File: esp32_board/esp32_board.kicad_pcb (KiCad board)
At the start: 2 copper layers, 57.2 x 63.5 mm, 6 parts, among them J1 Conn_01x06, Q1 2N5551, Q2 IRF5305

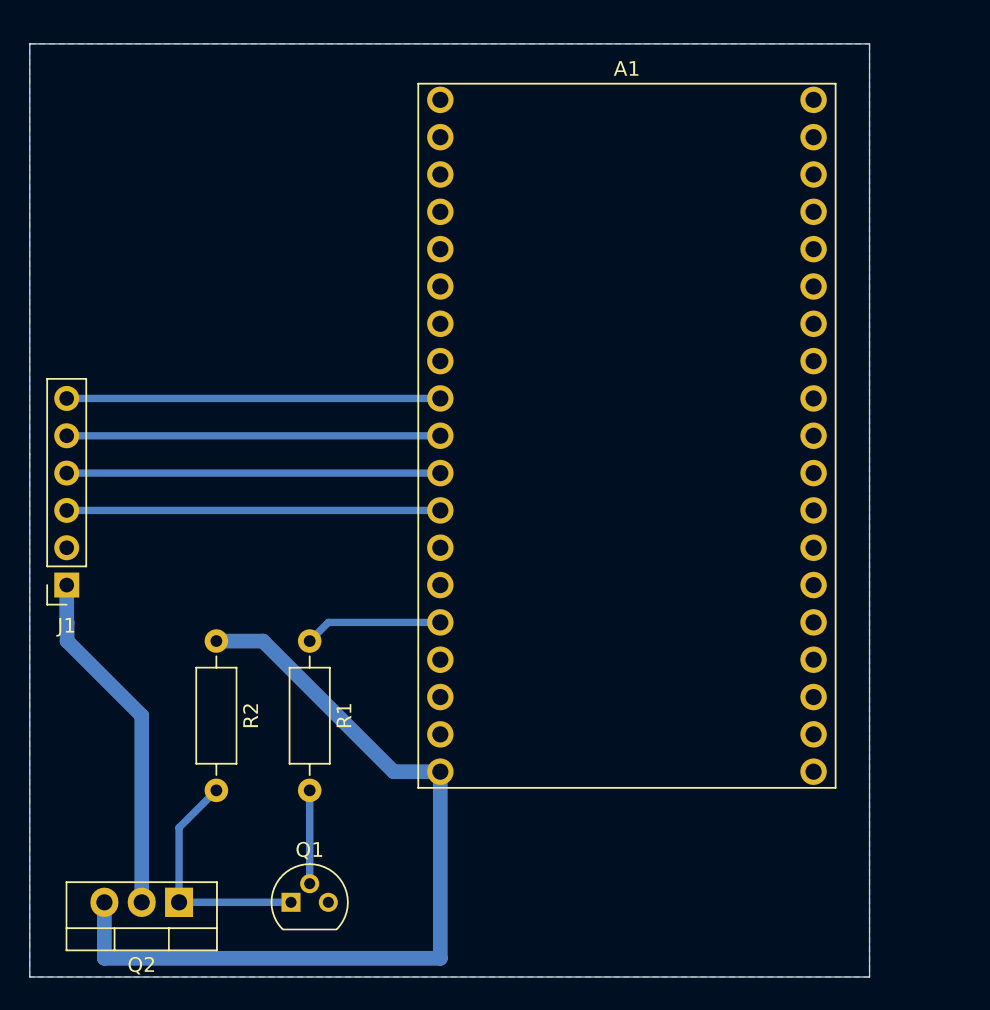
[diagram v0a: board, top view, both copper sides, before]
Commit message: Reduce PCB size to 50mmx50mm, set zone clearance to 1 mm
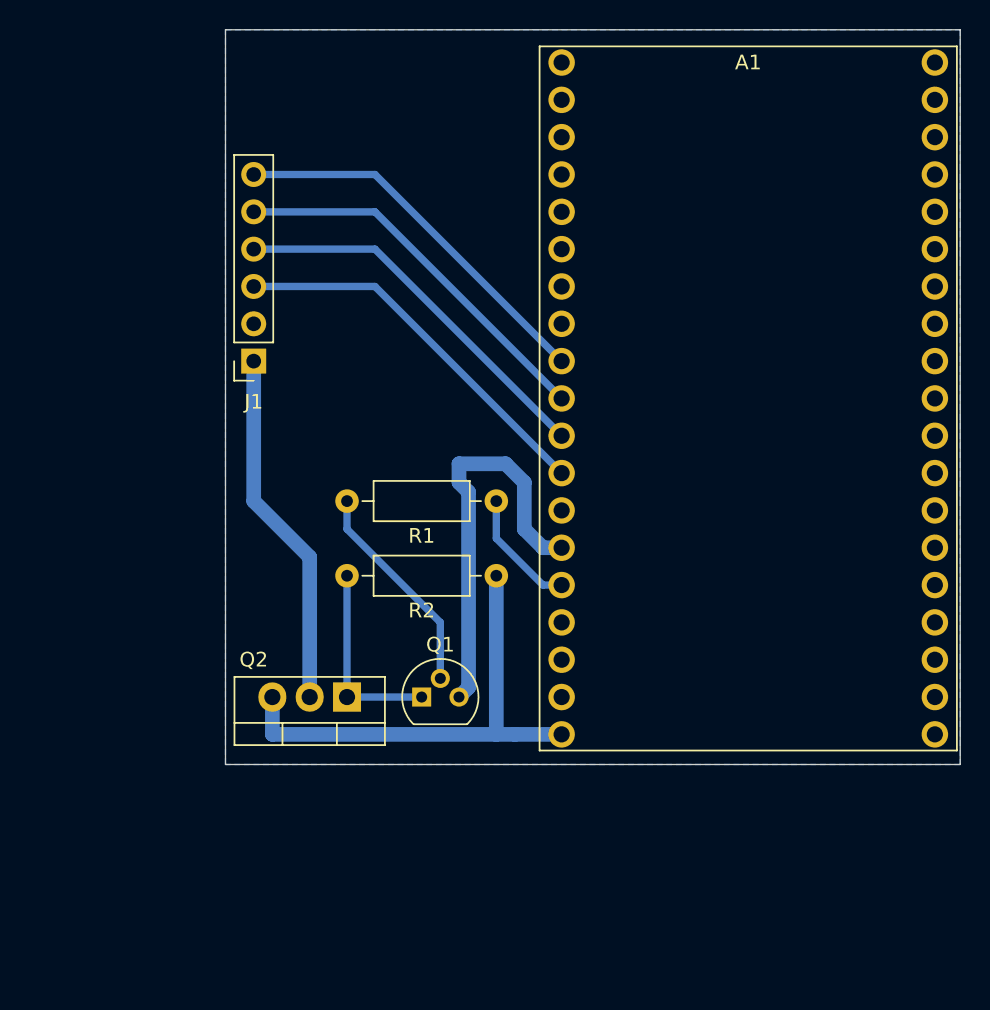
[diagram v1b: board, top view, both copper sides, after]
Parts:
- moved J1 19.9 mm to (121.9, 82.5)
- moved R2 19.6 mm to (138.4, 97.2), turned to 180 degrees
- moved Q2 18.1 mm to (128.3, 105.4)
- moved Q1 16.6 mm to (133.3, 105.4)
- moved R1 15.9 mm to (138.4, 92.1), turned to 180 degrees
- moved A1 8.64 mm to (155.6, 85.1)
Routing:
- net GND: track 0.00 -> 27.6 mm
- net +5V: track 58.3 -> 33.0 mm
- net Net-(Q1-B): track 6.35 -> 14.7 mm
- net Net-(Q1-C): track 16.3 -> 13.3 mm
- net /MISO: track 25.4 -> 26.9 mm
- net Net-(A1-IO13): track 9.42 -> 8.30 mm
- net /SCK: track 25.4 -> 26.2 mm
- net /MOSI: track 25.4 -> 26.2 mm
- net /CS: track 25.4 -> 26.2 mm
- net /FPGA_5V: track 23.7 -> 24.4 mm
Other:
- board size 57.2 x 63.5 mm -> 50 x 50 mm

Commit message: Connect all GND pins
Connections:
- A1 pad 32: unconnected-(A1-GND-Pad32) -> GND
- A1 pad 38: unconnected-(A1-GND-Pad38) -> GND
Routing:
- net GND: track 27.6 -> 78.3 mm

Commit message: Add mounting holes
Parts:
- added REF**: MountingHole_3.2mm_M3, MountingHole:MountingHole_3.2mm_M3, F.Cu at (161.3, 63.5)
- added REF**: MountingHole_3.2mm_M3, MountingHole:MountingHole_3.2mm_M3, F.Cu at (127.0, 63.5)
- added REF**: MountingHole_3.2mm_M3, MountingHole:MountingHole_3.2mm_M3, F.Cu at (161.3, 106.0)
